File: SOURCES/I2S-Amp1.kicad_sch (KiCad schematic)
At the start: 31 parts, among them P10 CONN_01X02, P17 MC4, P24 MP11, P25 MP6, P26 MP10, P9 CONN_01X02, U4 TAS5760MDCAR

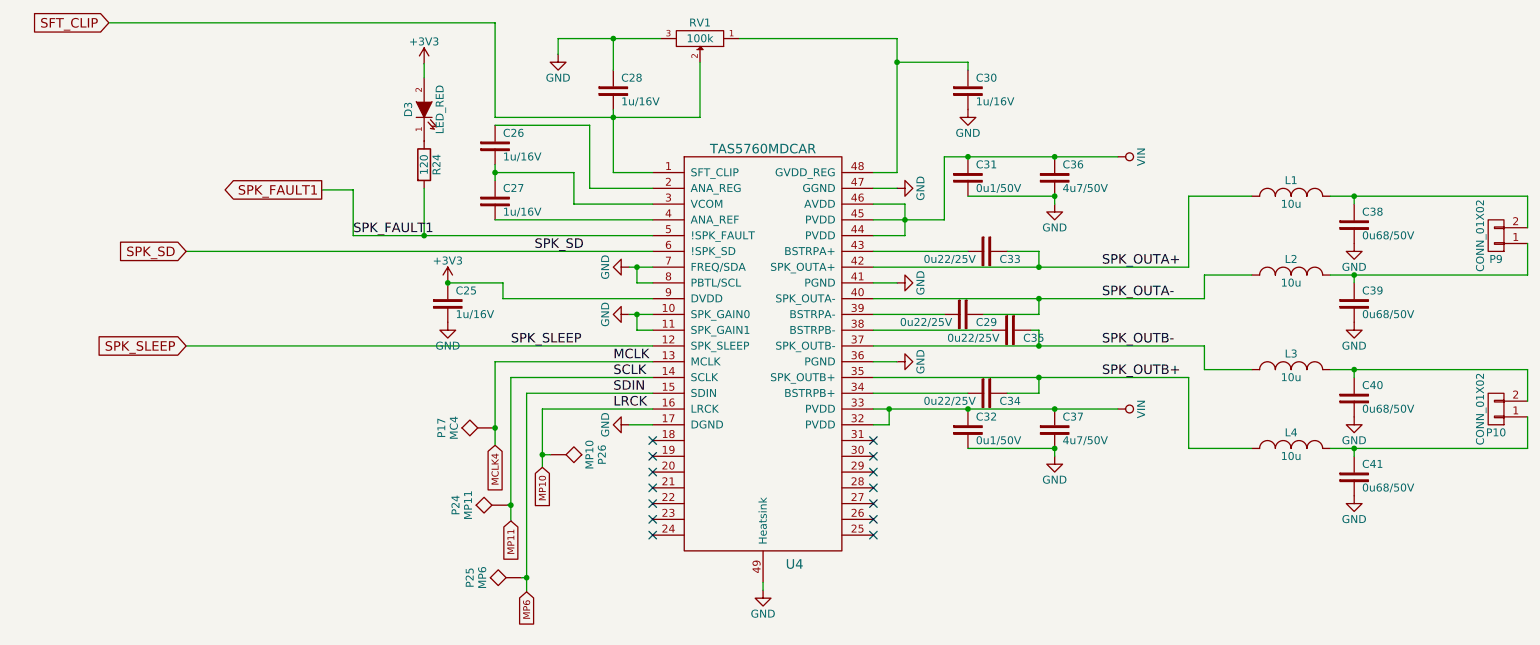
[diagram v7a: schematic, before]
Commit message: Improved power traces.
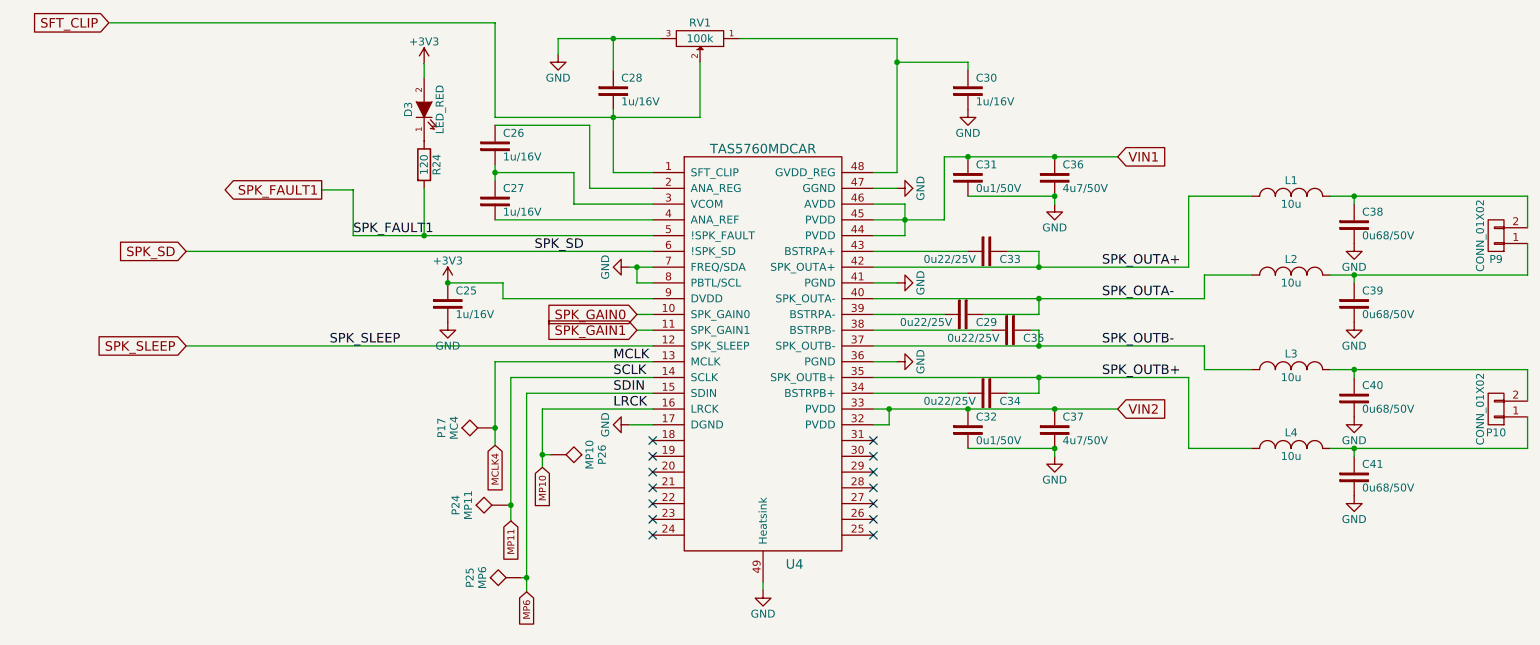
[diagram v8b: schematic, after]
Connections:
- net GND: no longer U4.10 (SPK_GAIN0), U4.11 (SPK_GAIN1)
- net VIN renamed VIN1
- net VIN1: no longer C32.1, C37.1, U4.32 (PVDD), U4.33 (PVDD)
- new net SPK_GAIN0: U4.10 (SPK_GAIN0)
- new net SPK_GAIN1: U4.11 (SPK_GAIN1)
- new net VIN2: C32.1, C37.1, U4.32 (PVDD), U4.33 (PVDD)
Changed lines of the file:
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@@
 	)
 	(junction
-		(at 125.73 71.12)
-		(diameter 0)
-		(color 0 0 0 0)
-	)
-	(junction
 		(at 168.91 55.88)
 		(diameter 0)
@@
 	(wire
 		(pts
+			(xy 125.73 73.66) (xy 128.27 73.66)
+		)
+		(stroke
+			(width 0)
+			(type default)
+		)
+	)
+	(wire
+		(pts
 			(xy 102.616 89.408) (xy 102.87 89.408)
 		)
@@
 	(wire
 		(pts
-			(xy 125.73 73.66) (xy 125.73 71.12)
-		)
-		(stroke
-			(width 0)
-			(type default)
-		)
-	)
-	(wire
-		(pts
 			(xy 107.95 83.82) (xy 107.95 113.538)
 		)
@@
 	(wire
 		(pts
-			(xy 124.46 71.12) (xy 125.73 71.12)
-		)
-		(stroke
-			(width 0)
-			(type default)
-		)
-	)
-	(wire
-		(pts
 			(xy 107.95 113.538) (xy 107.95 115.824)
 		)
@@
 	(wire
 		(pts
-			(xy 128.27 73.66) (xy 125.73 73.66)
-		)
-		(stroke
-			(width 0)
-			(type default)
-		)
-	)
-	(wire
-		(pts
 			(xy 237.49 80.01) (xy 241.3 80.01)
 		)
@@
 	(wire
 		(pts
-			(xy 102.87 89.408) (xy 102.87 92.202)
+			(xy 125.73 71.12) (xy 128.27 71.12)
 		)
 		(stroke
@@
 	(wire
 		(pts
-			(xy 125.73 71.12) (xy 128.27 71.12)
+			(xy 102.87 89.408) (xy 102.87 92.202)
 		)
 		(stroke
@@
 	)
 	(label "SPK_SLEEP"
-		(at 105.41 76.2 0)
+		(at 76.2 76.2 0)
 		(fields_autoplaced yes)
 		(effects
@@
 		)
 	)
+	(global_label "VIN2"
+		(shape input)
+		(at 203.2 86.36 0)
+		(fields_autoplaced yes)
+		(effects
+			(font
+				(size 1.524 1.524)
+			)
+			(justify left)
+		)
+		(property "Intersheetrefs" "${INTERSHEET_REFS}"
+			(at 211.0768 86.36 0)
+			(effects
+				(font
+					(size 1.27 1.27)
+				)
+				(justify left)
+				(hide yes)
+			)
+		)
+	)
 	(global_label "MCLK4"
 		(shape input)
@@
 		)
 	)
+	(global_label "SPK_GAIN1"
+		(shape input)
+		(at 125.73 73.66 180)
+		(fields_autoplaced yes)
+		(effects
+			(font
+				(size 1.524 1.524)
+			)
+			(justify right)
+		)
+		(property "Intersheetrefs" "${INTERSHEET_REFS}"
+			(at 110.6687 73.66 0)
+			(effects
+				(font
+					(size 1.27 1.27)
+				)
+				(justify right)
+				(hide yes)
+			)
+		)
+	)
+	(global_label "SPK_GAIN0"
+		(shape input)
+		(at 125.73 71.12 180)
+		(fields_autoplaced yes)
+		(effects
+			(font
+				(size 1.524 1.524)
+			)
+			(justify right)
+		)
+		(property "Intersheetrefs" "${INTERSHEET_REFS}"
+			(at 110.6687 71.12 0)
+			(effects
+				(font
+					(size 1.27 1.27)
+				)
+				(justify right)
+				(hide yes)
+			)
+		)
+	)
 	(global_label "SFT_CLIP"
 		(shape input)
@@
 		)
 	)
+	(global_label "VIN1"
+		(shape input)
+		(at 203.2 45.72 0)
+		(fields_autoplaced yes)
+		(effects
+			(font
+				(size 1.524 1.524)
+			)
+			(justify left)
+		)
+		(property "Intersheetrefs" "${INTERSHEET_REFS}"
+			(at 211.0768 45.72 0)
+			(effects
+				(font
+					(size 1.27 1.27)
+				)
+				(justify left)
+				(hide yes)
+			)
+		)
+	)
 	(global_label "MP11"
 		(shape input)
@@
 	(symbol
 		(lib_id "smd_aio-rescue:GND")
-		(at 124.46 71.12 270)
-		(unit 1)
-		(exclude_from_sim no)
-		(in_bom yes)
-		(on_board yes)
-		(dnp no)
-		(property "Reference" "#PWR055"
-			(at 118.11 71.12 0)
-			(effects
-				(font
-					(size 1.27 1.27)
-				)
-				(hide yes)
-			)
-		)
-		(property "Value" "GND"
-			(at 120.65 71.12 0)
-			(effects
-				(font
-					(size 1.27 1.27)
-				)
-			)
-		)
-		(property "Footprint" ""
-			(at 124.46 71.12 0)
-			(effects
-				(font
-					(size 1.27 1.27)
-				)
-			)
-		)
-		(property "Datasheet" ""
-			(at 124.46 71.12 0)
-			(effects
-				(font
-					(size 1.27 1.27)
-				)
-			)
-		)
-		(property "Description" ""
-			(at 124.46 71.12 0)
-			(effects
-				(font
-					(size 1.27 1.27)
-				)
-				(hide yes)
-			)
-		)
-		(pin "1"
-		)
-		(instances
-			(project "smd_aio"
-				(path "/4c49a07c-9ad4-4758-901a-e68e360dc17d/00000000-0000-0000-0000-00005af9ff80"
-					(reference "#PWR055")
-					(unit 1)
-				)
-			)
-		)
-	)
-	(symbol
-		(lib_id "smd_aio-rescue:GND")
 		(at 124.46 63.5 270)
 		(unit 1)
@@
 	)
 	(symbol
-		(lib_id "smd_aio-rescue:VCC")
-		(at 203.2 86.36 270)
-		(unit 1)
-		(exclude_from_sim no)
-		(in_bom yes)
-		(on_board yes)
-		(dnp no)
-		(property "Reference" "#PWR057"
-			(at 199.39 86.36 0)
-			(effects
-				(font
-					(size 1.27 1.27)
-				)
-				(hide yes)
-			)
-		)
-		(property "Value" "VIN"
-			(at 207.01 86.36 0)
-			(effects
-				(font
-					(size 1.27 1.27)
-				)
-			)
-		)
-		(property "Footprint" ""
-			(at 203.2 86.36 0)
-			(effects
-				(font
-					(size 1.27 1.27)
-				)
-			)
-		)
-		(property "Datasheet" ""
-			(at 203.2 86.36 0)
-			(effects
-				(font
-					(size 1.27 1.27)
-				)
-			)
-		)
-		(property "Description" ""
-			(at 203.2 86.36 0)
-			(effects
-				(font
-					(size 1.27 1.27)
-				)
-				(hide yes)
-			)
-		)
-		(pin "1"
-		)
-		(instances
-			(project "smd_aio"
-				(path "/4c49a07c-9ad4-4758-901a-e68e360dc17d/00000000-0000-0000-0000-00005af9ff80"
-					(reference "#PWR057")
-					(unit 1)
-				)
-			)
-		)
-	)
-	(symbol
 		(lib_id "smd_aio-rescue:R")
 		(at 91.44 46.99 0)
@@
 					(unit 1)
 				)
-			)
-		)
-	)
-	(symbol
-		(lib_id "smd_aio-rescue:VCC")
-		(at 203.2 45.72 270)
-		(unit 1)
-		(exclude_from_sim no)
-		(in_bom yes)
-		(on_board yes)
-		(dnp no)
-		(property "Reference" "#PWR061"
-			(at 199.39 45.72 0)
-			(effects
-				(font
-					(size 1.27 1.27)
-				)
-				(hide yes)
-			)
-		)
-		(property "Value" "VIN"
-			(at 207.01 45.72 0)
-			(effects
-				(font
-					(size 1.27 1.27)
-				)
-			)
-		)
-		(property "Footprint" ""
-			(at 203.2 45.72 0)
-			(effects
-				(font
-					(size 1.27 1.27)
-				)
-			)
-		)
-		(property "Datasheet" ""
-			(at 203.2 45.72 0)
-			(effects
-				(font
-					(size 1.27 1.27)
-				)
-			)
-		)
-		(property "Description" ""
-			(at 203.2 45.72 0)
-			(effects
-				(font
-					(size 1.27 1.27)
-				)
-				(hide yes)
-			)
-		)
-		(pin "1"
-		)
-		(instances
-			(project "smd_aio"
-				(path "/4c49a07c-9ad4-4758-901a-e68e360dc17d/00000000-0000-0000-0000-00005af9ff80"
-					(reference "#PWR061")
-					(unit 1)
-				)
